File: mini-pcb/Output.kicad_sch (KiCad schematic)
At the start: 13 parts, among them U2 OPA1664D

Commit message: almost done with mini pcb
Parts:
- removed R13, R14: 1M, Resistor_SMD:R_0603_1608Metric, symbol Device:R
- added R19: 39k, Resistor_SMD:R_0603_1608Metric, symbol Device:R
- added R20: 10k, Resistor_SMD:R_0603_1608Metric, symbol Device:R
- R5: value 1M -> 10k
- R8: value 1M -> 39k
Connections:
- net AUDIO_OUT_JACK_LEFT: no longer R8.2
- net at C9.1: now also U2.8, U2.9 (-); no longer R5.1
- net at C5.2, R3.2, R4.1: now also R19.2; no longer U2.10 (+)
- net at C3.2, R11.1, R12.2: now also R8.2; no longer U2.12 (+)
- net at C10.1: now also U2.13 (-), U2.14
- net AGND renamed GND
- net GND: now also R5.2, R20.2; no longer R8.1
- new net: R19.1, R5.1, U2.10 (+)
- new net: R20.1, R8.1, U2.12 (+)
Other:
- moved on the sheet: C10, C9, U2C, U2D

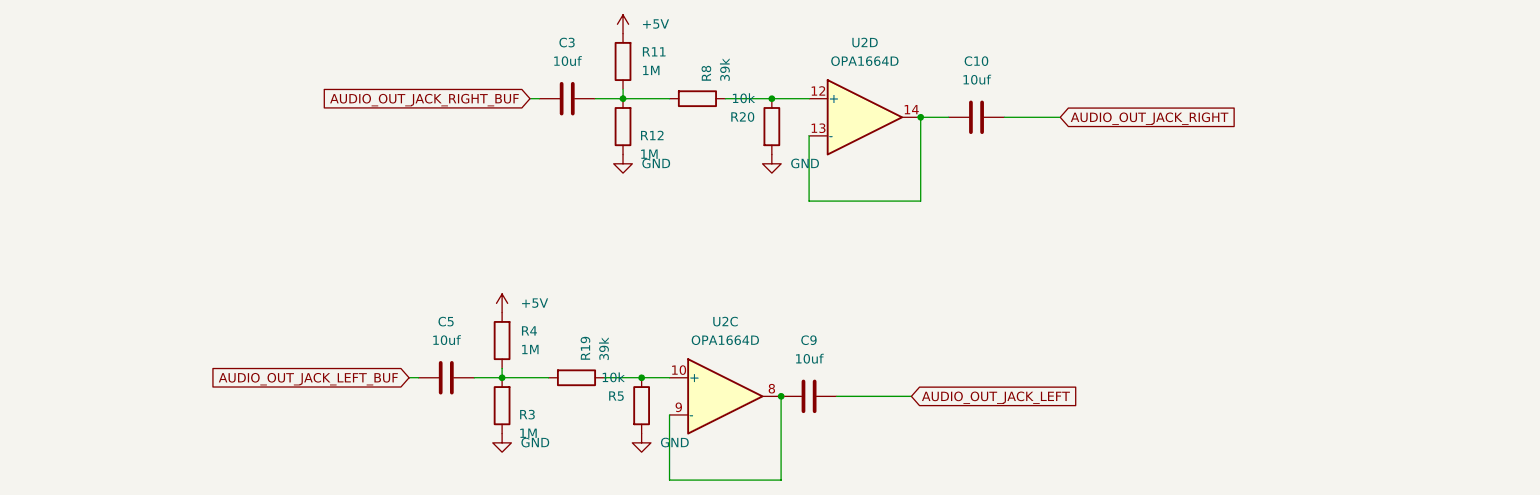
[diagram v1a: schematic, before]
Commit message: made final touches and bom still needs through testing
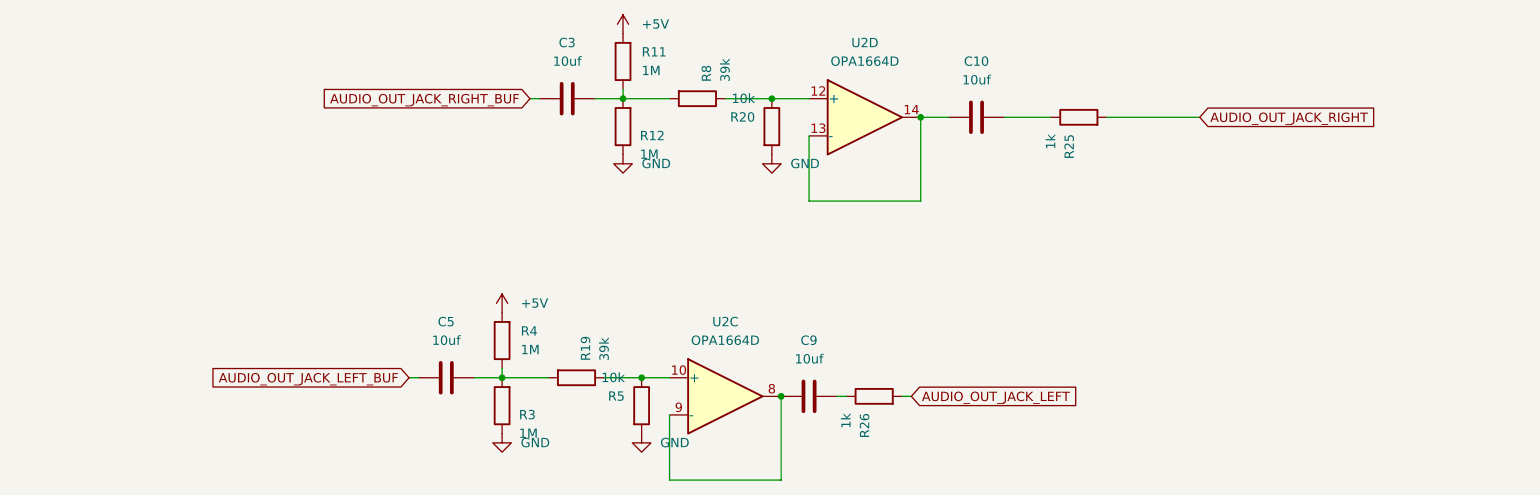
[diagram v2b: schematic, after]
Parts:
- added R25, R26: 1k, Resistor_SMD:R_0603_1608Metric, symbol Device:R
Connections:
- net AUDIO_OUT_JACK_LEFT: now also R26.2; no longer C9.2
- net AUDIO_OUT_JACK_RIGHT: now also R25.2; no longer C10.2
- new net: C9.2, R26.1
- new net: C10.2, R25.1
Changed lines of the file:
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@@
 	(wire
 		(pts
-			(xy 130.81 105.41) (xy 140.97 105.41)
+			(xy 130.81 105.41) (xy 132.08 105.41)
 		)
 		(stroke
@@
 	(wire
 		(pts
-			(xy 115.57 64.77) (xy 121.92 64.77)
+			(xy 139.7 105.41) (xy 140.97 105.41)
 		)
 		(stroke
@@
 	(wire
 		(pts
-			(xy 153.67 67.31) (xy 161.29 67.31)
+			(xy 115.57 64.77) (xy 121.92 64.77)
 		)
 		(stroke
@@
 	(wire
 		(pts
-			(xy 142.24 67.31) (xy 146.05 67.31)
+			(xy 153.67 67.31) (xy 160.02 67.31)
 		)
 		(stroke
@@
 	(wire
 		(pts
-			(xy 123.19 116.84) (xy 123.19 105.41)
+			(xy 142.24 67.31) (xy 146.05 67.31)
 		)
 		(stroke
@@
 	(wire
 		(pts
-			(xy 97.79 64.77) (xy 101.6 64.77)
+			(xy 123.19 116.84) (xy 123.19 105.41)
 		)
 		(stroke
@@
 		)
 	)
+	(wire
+		(pts
+			(xy 97.79 64.77) (xy 101.6 64.77)
+		)
+		(stroke
+			(width 0)
+			(type default)
+		)
+	)
+	(wire
+		(pts
+			(xy 167.64 67.31) (xy 180.34 67.31)
+		)
+		(stroke
+			(width 0)
+			(type default)
+		)
+	)
 	(global_label "AUDIO_OUT_JACK_RIGHT"
 		(shape input)
-		(at 161.29 67.31 0)
+		(at 180.34 67.31 0)
 		(fields_autoplaced yes)
 		(effects
@@
 		)
 		(property "Intersheetrefs" "${INTERSHEET_REFS}"
-			(at 186.4701 67.31 0)
+			(at 205.5201 67.31 0)
 			(effects
 				(font
@@
 	(symbol
 		(lib_id "Device:R")
+		(at 163.83 67.31 90)
+		(unit 1)
+		(exclude_from_sim no)
+		(in_bom yes)
+		(on_board yes)
+		(dnp no)
+		(property "Reference" "R25"
+			(at 162.56 69.596 0)
+			(effects
+				(font
+					(size 1.27 1.27)
+				)
+				(justify right)
+			)
+		)
+		(property "Value" "1k"
+			(at 160.02 69.596 0)
+			(effects
+				(font
+					(size 1.27 1.27)
+				)
+				(justify right)
+			)
+		)
+		(property "Footprint" "Resistor_SMD:R_0603_1608Metric"
+			(at 163.83 69.088 90)
+			(effects
+				(font
+					(size 1.27 1.27)
+				)
+				(hide yes)
+			)
+		)
+		(property "Datasheet" "~"
+			(at 163.83 67.31 0)
+			(effects
+				(font
+					(size 1.27 1.27)
+				)
+				(hide yes)
+			)
+		)
+		(property "Description" "Resistor"
+			(at 163.83 67.31 0)
+			(effects
+				(font
+					(size 1.27 1.27)
+				)
+				(hide yes)
+			)
+		)
+		(pin "2"
+		)
+		(pin "1"
+		)
+		(instances
+			(project "mini_pcb"
+				(path "/ac8ee366-0662-41f8-9745-078ec3fbb21b/71b17037-91e4-4ab7-a98f-0d6408c65901"
+					(reference "R25")
+					(unit 1)
+				)
+			)
+		)
+	)
+	(symbol
+		(lib_id "Device:R")
 		(at 121.92 68.58 0)
 		(unit 1)
@@
 					(unit 1)
 				)
+			)
+		)
+	)
+	(symbol
+		(lib_id "Device:R")
+		(at 135.89 105.41 90)
+		(unit 1)
+		(exclude_from_sim no)
+		(in_bom yes)
+		(on_board yes)
+		(dnp no)
+		(property "Reference" "R26"
+			(at 134.62 107.696 0)
+			(effects
+				(font
+					(size 1.27 1.27)
+				)
+				(justify right)
+			)
+		)
+		(property "Value" "1k"
+			(at 132.08 107.696 0)
+			(effects
+				(font
+					(size 1.27 1.27)
+				)
+				(justify right)
+			)
+		)
+		(property "Footprint" "Resistor_SMD:R_0603_1608Metric"
+			(at 135.89 107.188 90)
+			(effects
+				(font
+					(size 1.27 1.27)
+				)
+				(hide yes)
+			)
+		)
+		(property "Datasheet" "~"
+			(at 135.89 105.41 0)
+			(effects
+				(font
+					(size 1.27 1.27)
+				)
+				(hide yes)
+			)
+		)
+		(property "Description" "Resistor"
+			(at 135.89 105.41 0)
+			(effects
+				(font
+					(size 1.27 1.27)
+				)
+				(hide yes)
+			)
+		)
+		(pin "2"
+		)
+		(pin "1"
+		)
+		(instances
+			(project "mini_pcb"
+				(path "/ac8ee366-0662-41f8-9745-078ec3fbb21b/71b17037-91e4-4ab7-a98f-0d6408c65901"
+					(reference "R26")
+					(unit 1)
+				)

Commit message: ordered pcb
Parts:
- removed C10: 10uf, Capacitor_SMD:C_0805_2012Metric, symbol Device:C
- removed R11, R12, R3, R4: 1M, Resistor_SMD:R_0603_1608Metric, symbol Device:R
- removed R19, R8: 39k, Resistor_SMD:R_0603_1608Metric, symbol Device:R
- removed R20, R5: 10k, Resistor_SMD:R_0603_1608Metric, symbol Device:R
- added C16, C17: 1nf, Capacitor_SMD:C_0805_2012Metric, symbol Device:C
- added C6: 10uf, Capacitor_SMD:C_0805_2012Metric, symbol Device:C
- added R2, R9: 7.5k, Resistor_SMD:R_0603_1608Metric, symbol Device:R
- added R6, R7: 100, Resistor_SMD:R_0603_1608Metric, symbol Device:R
- C3, C5, C9: MPN (none) -> C440198
- R25, R26: value 1k -> 100; MPN (none) -> C22775
- U2: MPN (none) -> C69414
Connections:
- net AUDIO_OUT_JACK_LEFT_BUF: now also R6.1; no longer C5.1
- net AUDIO_OUT_JACK_RIGHT_BUF: now also R7.1; no longer C3.1
- net GND: now also C16.1, C17.1
- net at U2.8, U2.9 (-): now also R2.1; no longer C9.1
- net at C9.2: now also R25.1; no longer R26.1
- net at C5.2: now also U2.10 (+)
- net at C3.2: now also U2.12 (+)
- net at U2.13 (-), U2.14: now also R9.1
- new net: C5.1, R6.2
- new net: C17.2, C9.1, R9.2
- new net: C6.2, R26.1
- new net: C3.1, R7.2
- new net: C16.2, C6.1, R2.2
